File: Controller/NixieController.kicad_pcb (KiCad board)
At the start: 2 copper layers, 180 x 41 mm, 101 parts, among them J1 Conn_01x12_Male, J2 Conn_01x12_Male, J3 Conn_01x12_Male, J4 Conn_01x12_Male, J5 Conn_01x12_Male, J6 Conn_01x12_Male, J7 Jack-DC, J8 Conn_01x02_Male, J9 Conn_01x06_Male, Q1 IRF644, Q10 BSS127, Q11 BSS127, Q12 BSS127, Q13 BSS127, Q14 BSS127, Q15 BSS127, Q16 BSS127, Q17 BSS127, Q18 BSS127, Q19 BSS127, Q2 BSS127, Q20 BSS127, Q21 BSS127, Q22 BSS127, Q23 BSS127, Q24 BSS127, Q25 BSS127, Q26 BSS127, Q27 BSS127, Q28 BSS127, Q29 BSS127, Q3 BSS127, Q30 BSS127, Q31 BSS127, Q32 BSS127, Q33 BSS127, Q34 BSS127, Q35 BSS127, Q36 BSS127, Q37 BSS127, Q38 BSS127, Q39 BSS127, Q4 BSS127, Q40 BSS127, Q41 BSS127, Q42 BSS127, Q43 BSS127, Q44 BSS127, Q45 BSS127, Q46 BSS127, Q47 BSS127, Q48 BSS127, Q49 BSS127, Q5 BSS127, Q50 BSS127, Q51 BSS127, Q52 BSS127, Q53 BSS127, Q54 BSS127, Q55 BSS127, Q56 BSS127, Q57 BSS127, Q58 BSS127, Q59 BSS127, Q6 BSS127, Q60 BSS127, Q61 BSS127, Q7 BSS127, Q8 BSS127, Q9 BSS127, U1 ATtiny85-20SU, U10 74HC595, U11 74HC595, U12 74HC595, U2 DS1307Z+, U3 LM2576, U4 MAX1771, U5 74HC595, U6 74HC595, U7 74HC595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

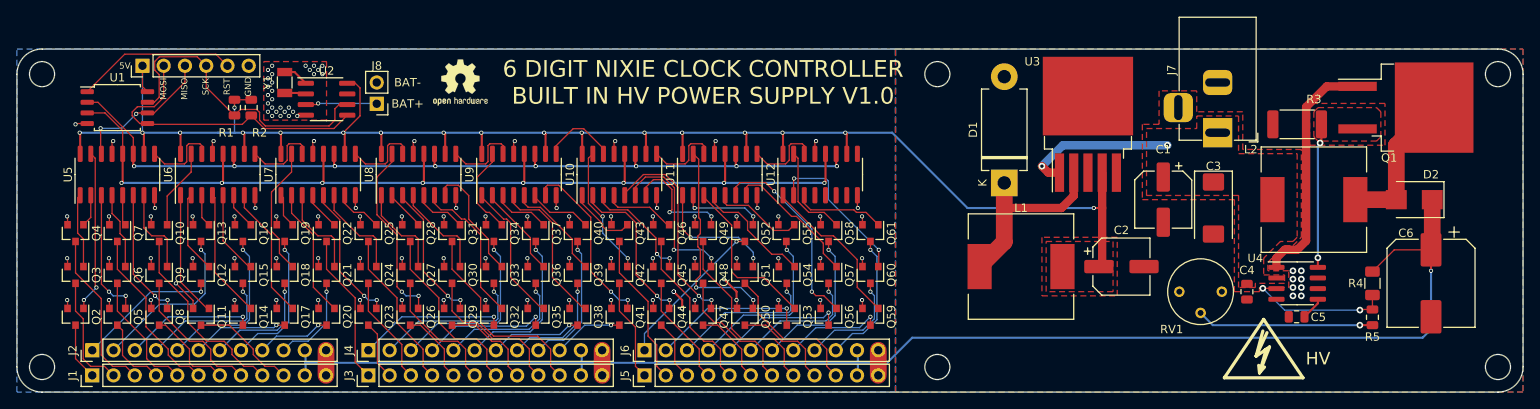
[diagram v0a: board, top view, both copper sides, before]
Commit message: Add github link to controller, fix ground plane issues
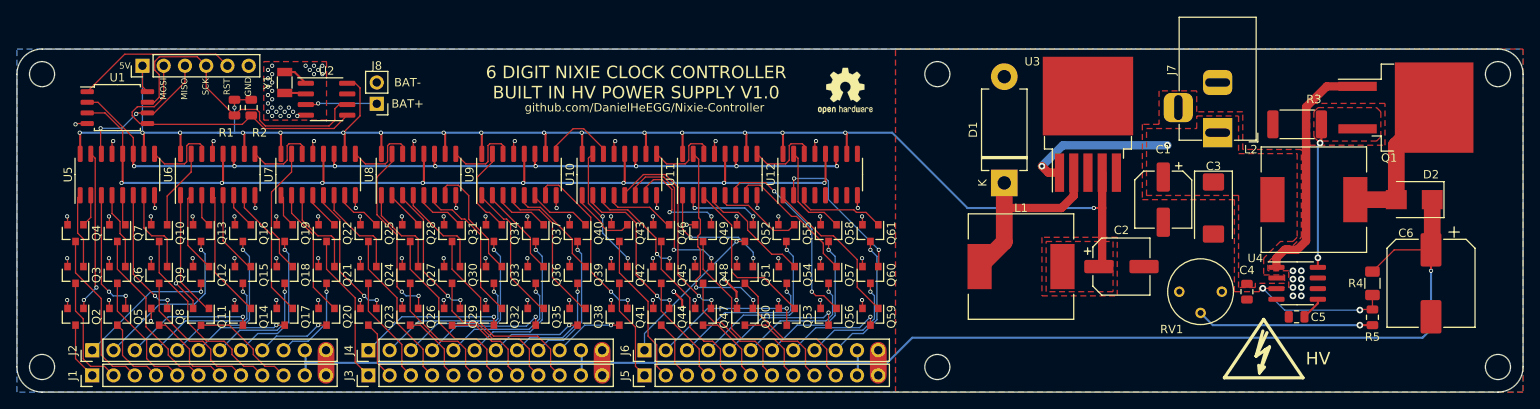
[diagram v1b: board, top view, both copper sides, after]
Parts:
- moved REF** 46.0 mm to (159.0, 80.0)
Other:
- board text added: "github.com/DanielHeEGG/Nixie-Controller"

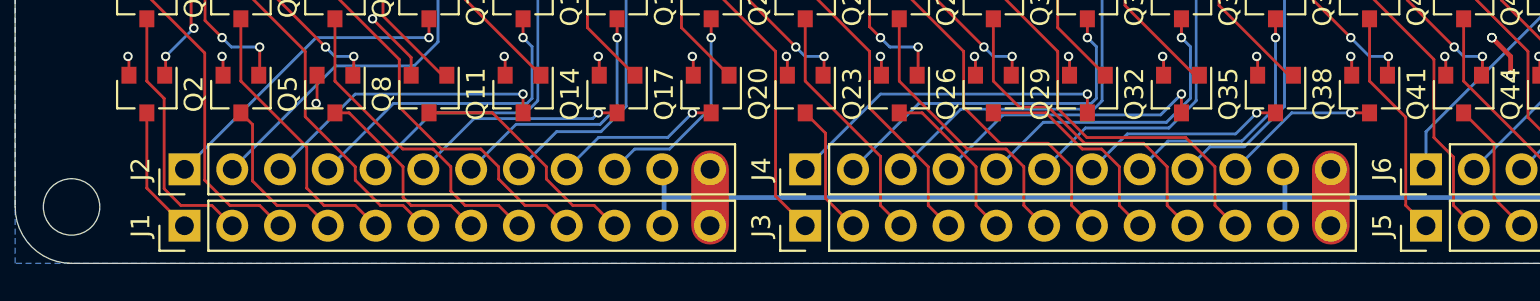
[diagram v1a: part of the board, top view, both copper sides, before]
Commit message: Change pin header on controller from male to female
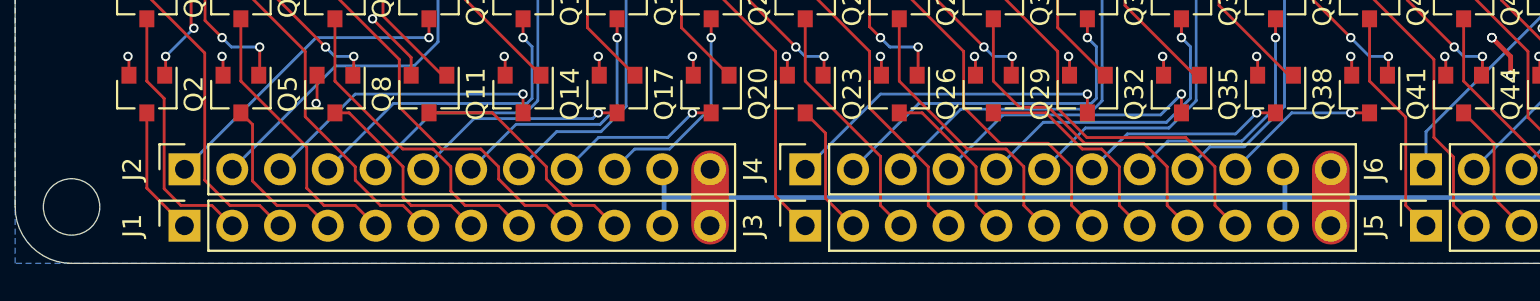
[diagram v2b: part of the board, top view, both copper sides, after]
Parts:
- J1, J2, J3, J4, J5, J6: value Conn_01x12_Male -> Conn_01x12_Female; footprint Connector_PinHeader_2.54mm:PinHeader_1x12_P2.54mm_Vertical -> Connector_PinSocket_2.54mm:PinSocket_1x12_P2.54mm_Vertical

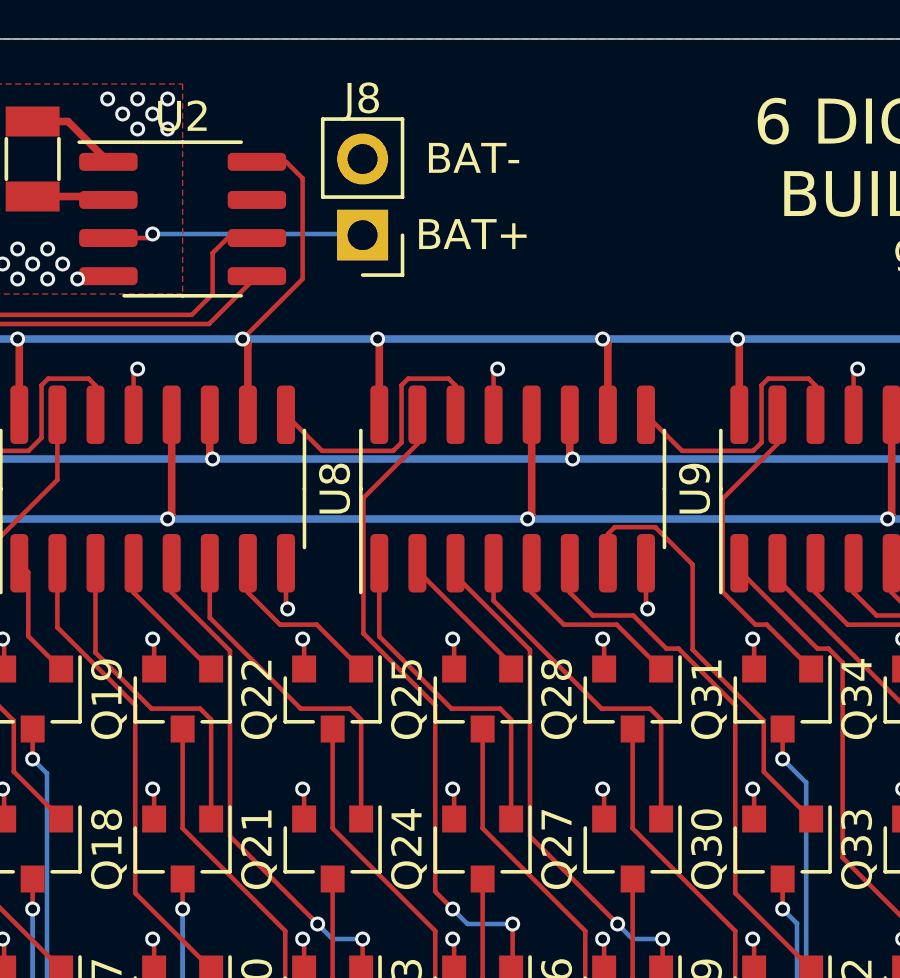
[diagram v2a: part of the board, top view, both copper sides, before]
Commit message: Add battery mount to controller
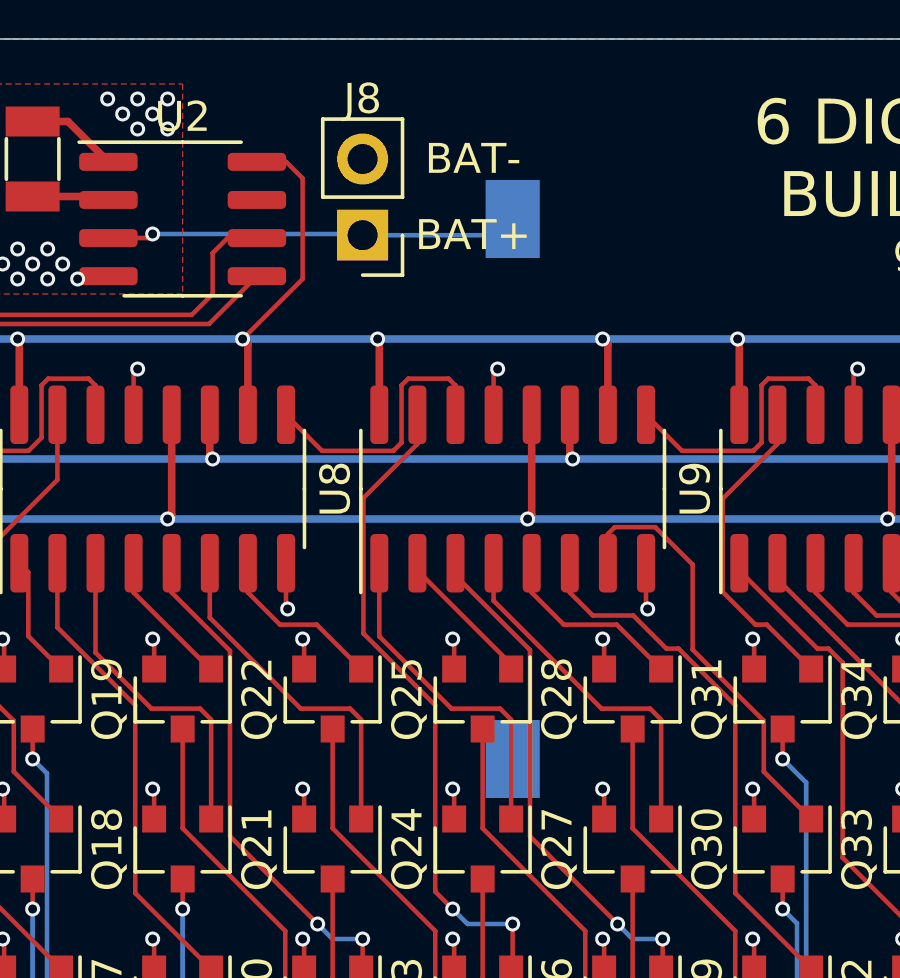
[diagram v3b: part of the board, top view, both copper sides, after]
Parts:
- added BT1: Battery_Cell, NixieController:Keystone_1056, B.Cu at (108.0, 90.0)
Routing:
- net Net-(BT1-Pad1): track 8.55 -> 13.8 mm

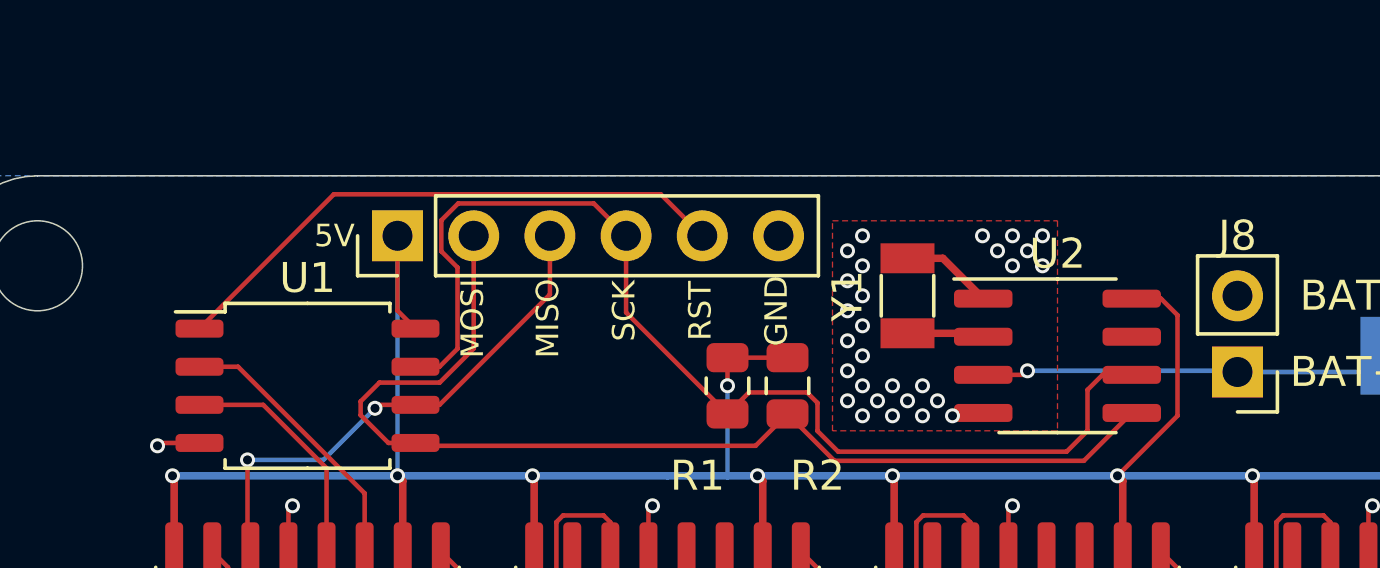
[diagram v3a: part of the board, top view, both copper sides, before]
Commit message: Add bypass caps for micro and RTC
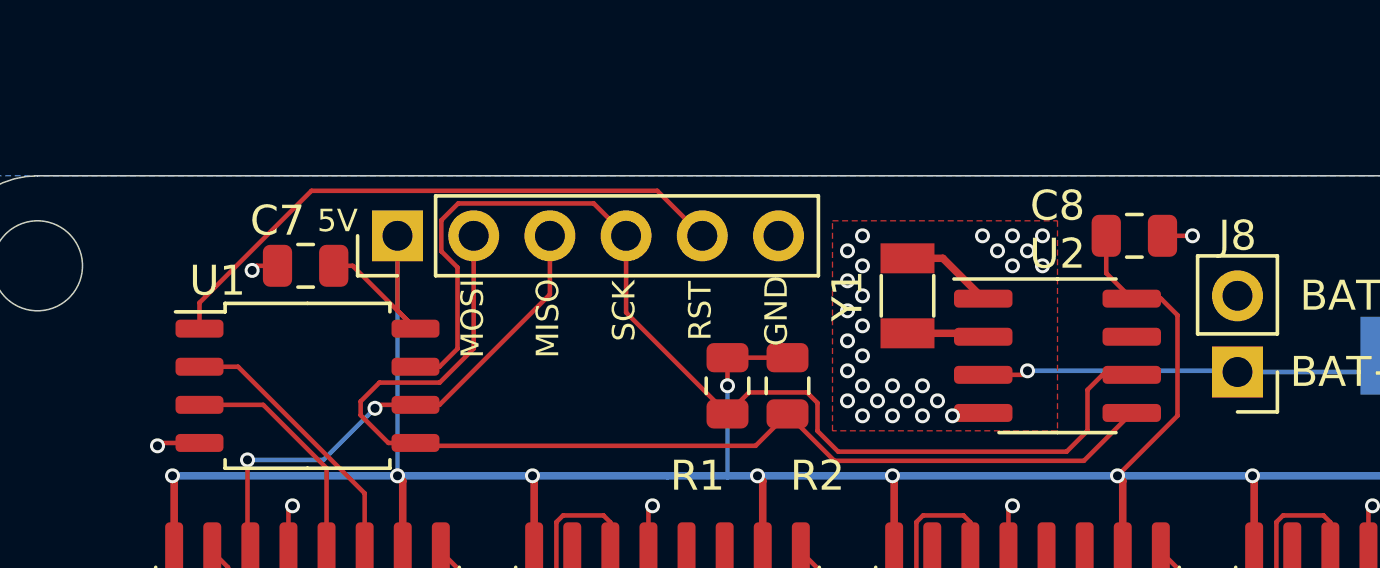
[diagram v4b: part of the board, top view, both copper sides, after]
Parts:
- added C7: 100nF, Capacitor_SMD:C_0805_2012Metric, F.Cu at (71.9, 78.0)
- added C8: 100nF, Capacitor_SMD:C_0805_2012Metric, F.Cu at (99.6, 77.0)
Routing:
- net +5V: track 203.7 -> 209.7 mm
- net GND: track 105.6 -> 107.5 mm, vias 117 -> 119
- net /RST: track 19.2 -> 19.8 mm
